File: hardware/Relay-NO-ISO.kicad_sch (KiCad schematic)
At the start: 10 parts, among them K13 G5V-1, Q13 2N3904

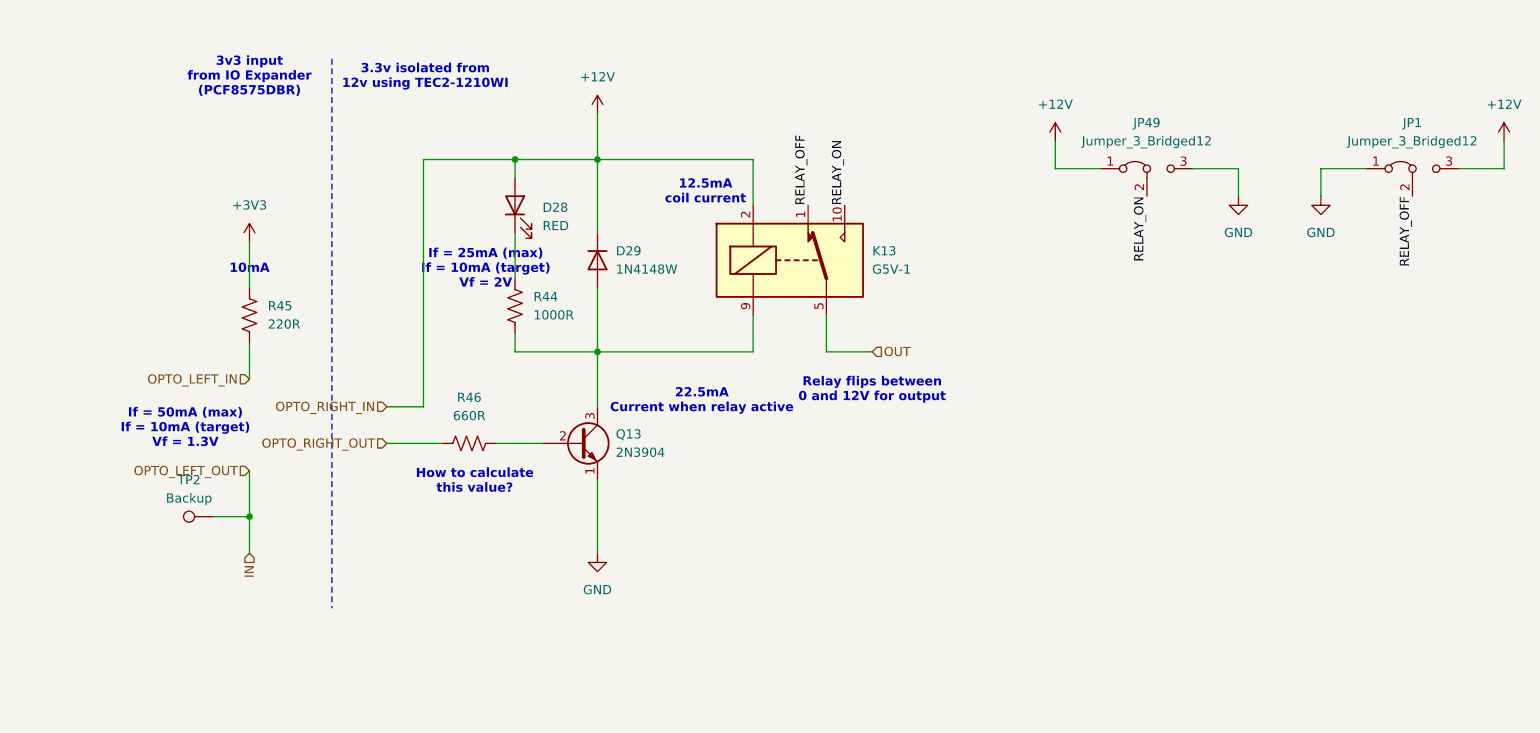
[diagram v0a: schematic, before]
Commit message: Transitioning to more robust circuit
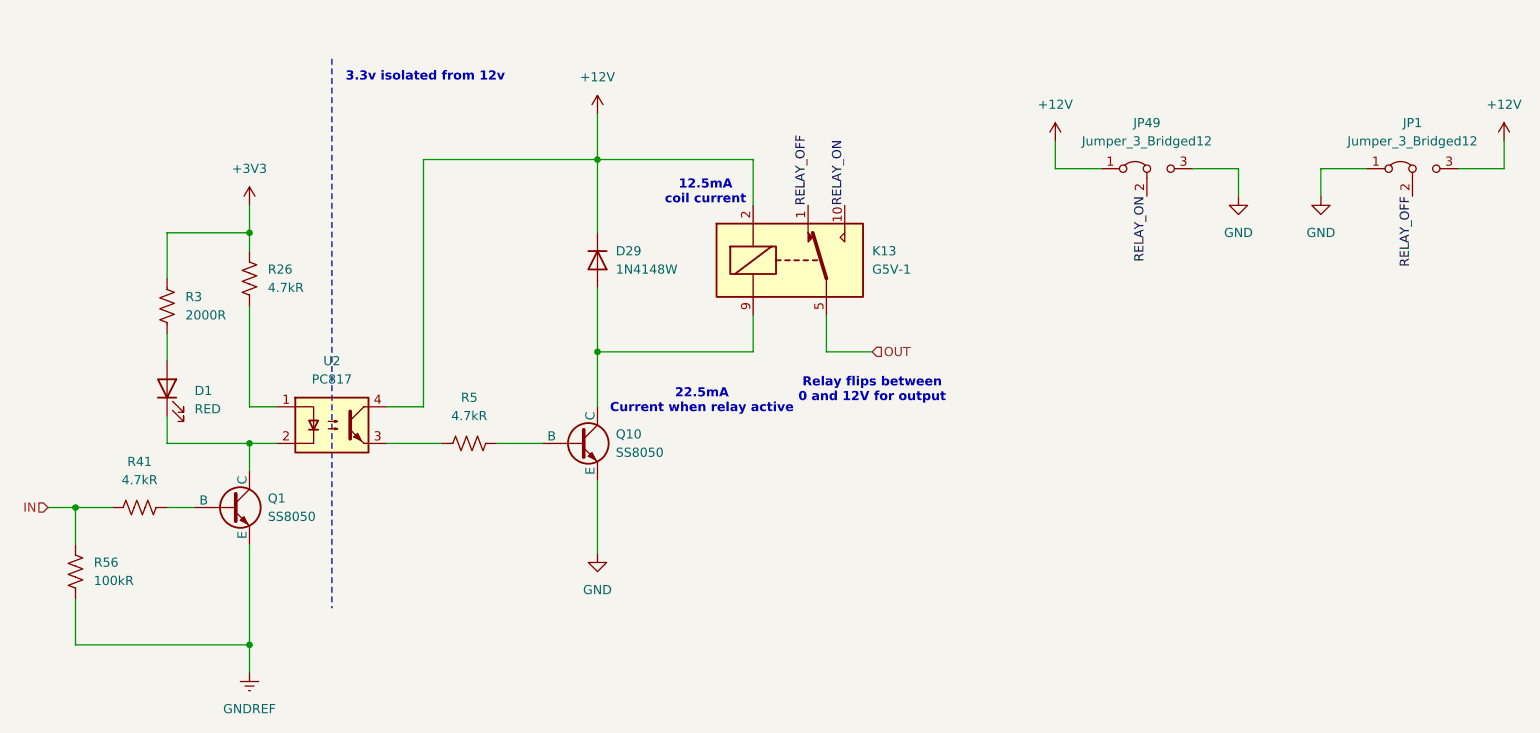
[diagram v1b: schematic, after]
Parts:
- removed D28: RED, LED_SMD:LED_0805_2012Metric, symbol Device:LED
- removed Q13: 2N3904, Package_TO_SOT_SMD:SOT-23, symbol Transistor_BJT:2N3904
- removed R44: 1000R, Resistor_SMD:R_0603_1608Metric, symbol Device:R_US
- removed R45: 220R, Resistor_SMD:R_0603_1608Metric, symbol Device:R_US
- removed R46: 660R, Resistor_SMD:R_0603_1608Metric, symbol Device:R_US
- removed TP2: Backup, TestPoint:TestPoint_Pad_D1.0mm, symbol Connector:TestPoint
- added D1: RED, LED_SMD:LED_0805_2012Metric, symbol Device:LED
- added Q1, Q10: SS8050, Package_TO_SOT_SMD:SOT-23, symbol Simulation_SPICE:NPN
- added R26, R41, R5: 4.7kR, Resistor_SMD:R_0603_1608Metric, symbol Device:R_US
- added R3: 2000R, Resistor_SMD:R_0603_1608Metric, symbol Device:R_US
- added R56: 100kR, Resistor_SMD:R_0603_1608Metric, symbol Device:R_US
- added U2: PC817, Package_DIP:DIP-4_W7.62mm, symbol Isolator:PC817
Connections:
- net +12V: now also U2.4
- net +3V3: now also R26.1, R3.1
- net GND: now also Q10.2 (E)
- net IN: now also R41.1, R56.2
- net at D29.2 (A), K13.9: now also Q10.3 (C)
- new net: R5.1, U2.3
- new net: Q10.1 (B), R5.2
- new net: D1.1 (K), Q1.3 (C), U2.2
- new net: D1.2 (A), R3.2
- new net: Q1.1 (B), R41.2
- new net: R26.2, U2.1
- new net GNDREF: Q1.2 (E), R56.1
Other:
- note added: "3.3v isolated from 12v"
- note removed: "10mA"
- note removed: "3.3v isolated from 12v using TEC2-1210WI"
- note removed: "3v3 input from IO Expander (PCF8575DBR)"
- note removed: "How to calculate this value?"
- note removed: "If = 25mA (max) If = 10mA (target) Vf = 2V"
- note removed: "If = 50mA (max) If = 10mA (target) Vf = 1.3V"

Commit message: It could work but it's too big
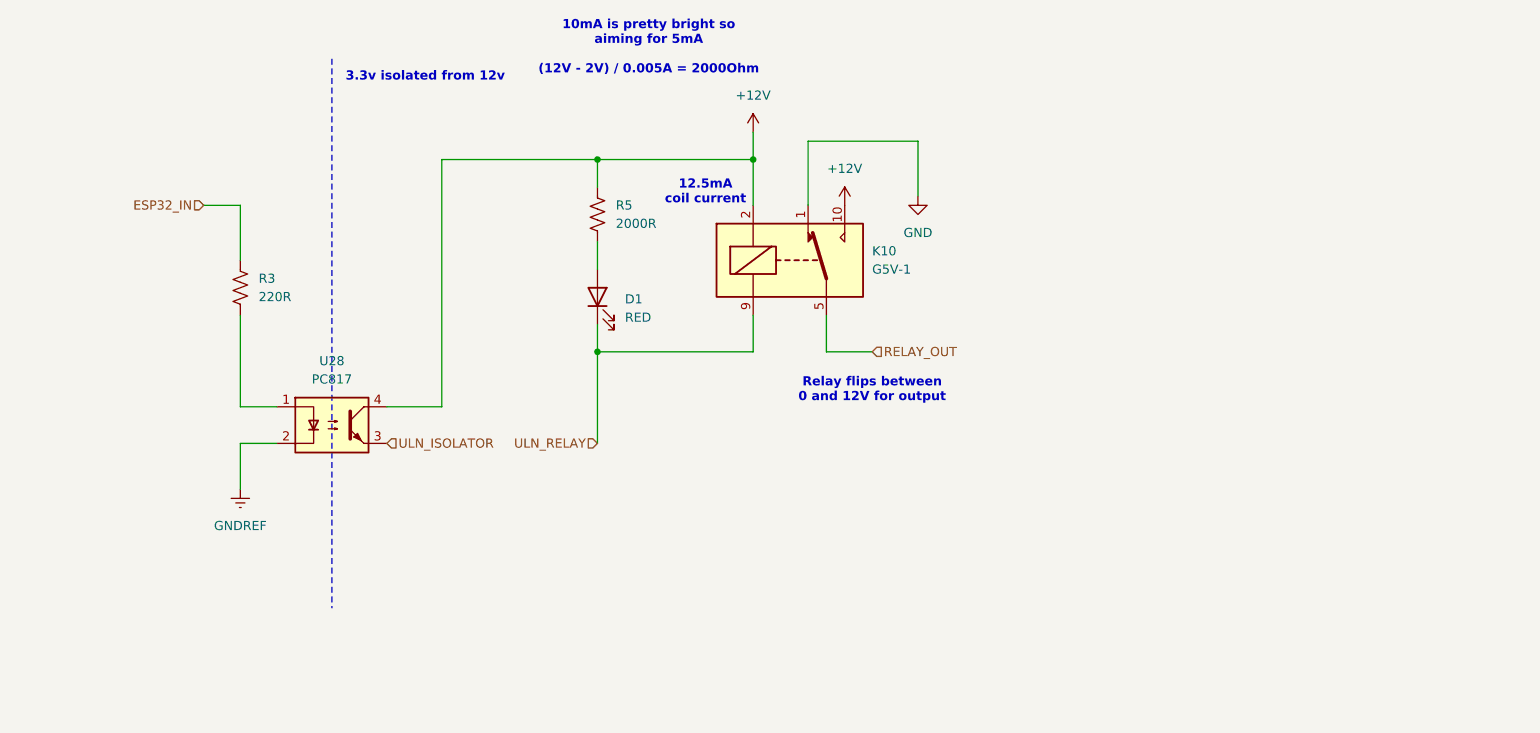
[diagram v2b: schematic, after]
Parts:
- removed D29: 1N4148W, Diode_SMD:D_SOD-123, symbol Device:D
- removed JP1, JP49: Jumper_3_Bridged12, Jumper:SolderJumper-3_P1.3mm_Bridged2Bar12_RoundedPad1.0x1.5mm, symbol Jumper:Jumper_3_Bridged12
- removed Q1, Q10: SS8050, Package_TO_SOT_SMD:SOT-23, symbol Simulation_SPICE:NPN
- removed R26, R41: 4.7kR, Resistor_SMD:R_0603_1608Metric, symbol Device:R_US
- removed R56: 100kR, Resistor_SMD:R_0603_1608Metric, symbol Device:R_US
- removed U2: PC817, Package_DIP:DIP-4_W7.62mm, symbol Isolator:PC817
- added U28: PC817, Package_DIP:DIP-4_W7.62mm_SMDSocket_SmallPads, symbol Isolator:PC817
- R3: value 2000R -> 220R; LCSC C22975 -> C22962
- R5: value 4.7kR -> 2000R; LCSC C23162 -> C22975
- renumbered K13 to K10
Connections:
- net RELAY_OFF is gone; now on net GND: K10.1
- net RELAY_ON is gone; now on net +12V: K10.10
- net +12V: now also R5.1, U28.4
- net GNDREF: now also U28.2
- net at R5.2: now also D1.2 (A)
- net ULN_RELAY: now reaches D1.1 (K)
- net ULN_RELAY: now also K10.9
- net at R3.2: now also U28.1; no longer D1.2 (A)
- net +3V3 renamed ESP32_IN
- net OUT renamed RELAY_OUT
- new net ULN_ISOLATOR: U28.3
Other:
- note added: "10mA is pretty bright so aiming for 5mA (12V - 2V) / 0.005A = 2000Ohm"
- note removed: "22.5mA Current when relay active"

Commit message: Schematic ready
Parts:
- removed R3: 220R, Resistor_SMD:R_0603_1608Metric, symbol Device:R_US
- removed U28: PC817, Package_DIP:DIP-4_W7.62mm_SMDSocket_SmallPads, symbol Isolator:PC817
